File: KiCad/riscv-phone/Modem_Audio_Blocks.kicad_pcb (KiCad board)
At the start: 2 copper layers, 45.6 x 58.7 mm, 42 parts, among them J1 Conn_01x08, J10 SIM_Card, J2 Conn_01x02, J3 Conn_01x05, J4 Conn_02x03_Odd_Even, J5 Conn_01x02, J6 Conn_01x02, J7 Conn_01x02, J8 Conn_01x02, J9 SJ-3524-SMT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

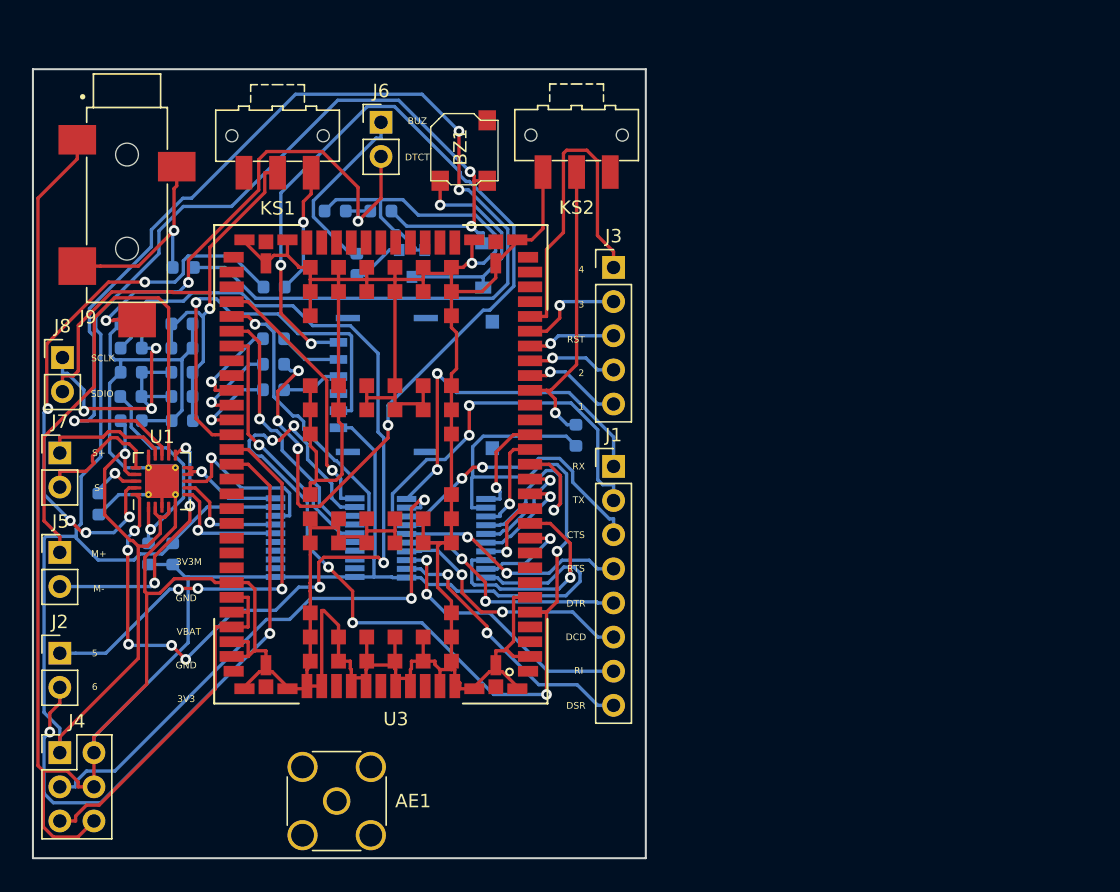
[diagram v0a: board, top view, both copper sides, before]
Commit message: Added GND planes and mounting holes
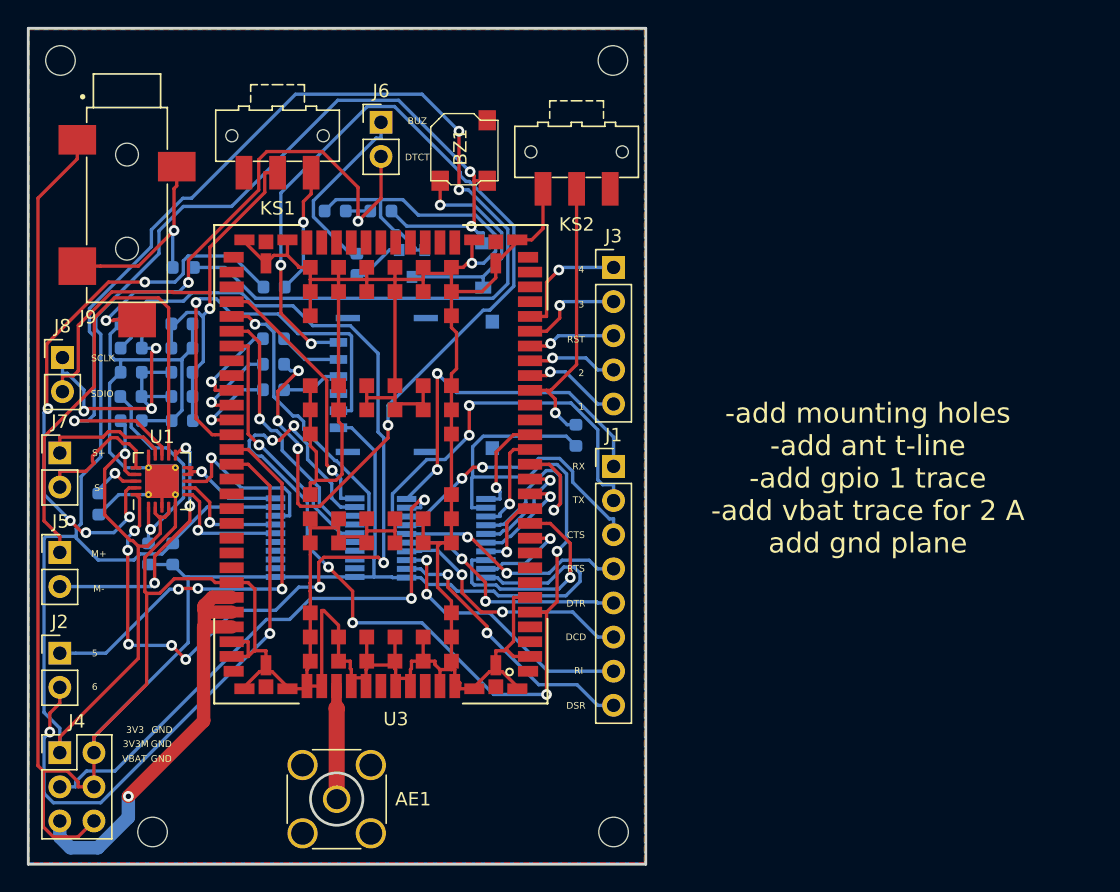
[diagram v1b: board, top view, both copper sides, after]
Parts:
- added ?: MountingHole_2.2mm_M2_ISO7380, MountingHole:MountingHole_2.2mm_M2_ISO7380, F.Cu at (106.0, 66.2)
- added ?: MountingHole_2.2mm_M2_ISO7380, MountingHole:MountingHole_2.2mm_M2_ISO7380, F.Cu at (147.2, 66.2)
- added ?: MountingHole_2.2mm_M2_ISO7380, MountingHole:MountingHole_2.2mm_M2_ISO7380, F.Cu at (147.2, 123.6)
- added ?: MountingHole_2.2mm_M2_ISO7380, MountingHole:MountingHole_2.2mm_M2_ISO7380, F.Cu at (112.9, 123.6)
- moved KS2 1.25 mm to (144.4, 73.0)
- moved AE1 0.14 mm to (126.6, 121.2)
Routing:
- net /ModemINDIV/GPIO4: track 25.3 -> 9.48 mm, vias 0 -> 1
- net Net-(AE1-Pad1): track 0.00 -> 8.44 mm
- net /ModemINDIV/VBAT: track 27.6 -> 33.1 mm, vias 0 -> 1
- net Net-(KS2-Pad2): track 22.4 -> 21.2 mm
- net GND: track 446.0 -> 444.8 mm
- added copper zone on B.Cu, net GND
- added copper zone on F.Cu, net GND
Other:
- board size 45.6 x 58.7 mm -> 45.9 x 62.2 mm
- board text added: "-add mounting holes -add ant t-line -add gpio 1 trace -add vbat trace for 2 A add gnd plane"

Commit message: Added GND vias
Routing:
- net GND: vias 1 -> 103
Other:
- outline, holes or cut-outs redrawn
- board text removed: "-add mounting holes -add ant t-line -add gpio 1 trace -add vbat trace for 2 A add gnd plane"

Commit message: Final PCB with added changes
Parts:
- removed ? (x4): MountingHole_2.2mm_M2_ISO7380, MountingHole:MountingHole_2.2mm_M2_ISO7380
- removed J5: Conn_01x02, Connector_PinHeader_2.54mm:PinHeader_1x02_P2.54mm_Vertical
- added Q2: MMBT3904, Package_TO_SOT_SMD:SOT-23, B.Cu at (133.4, 81.7)
- added R11: 1k, Resistor_SMD:R_0603_1608Metric, B.Cu at (133.4, 79.2)
- added R9: 1k, Resistor_SMD:R_0603_1608Metric, B.Cu at (133.2, 84.2)
- added m1: MountingHole_2.2mm_M2_ISO7380, MountingHole:MountingHole_2.2mm_M2_ISO7380, F.Cu at (146.8, 67.2)
- added m2: MountingHole_2.2mm_M2_ISO7380, MountingHole:MountingHole_2.2mm_M2_ISO7380, F.Cu at (105.9, 67.2)
- added m3: MountingHole_2.2mm_M2_ISO7380, MountingHole:MountingHole_2.2mm_M2_ISO7380, F.Cu at (105.9, 123.8)
- added m4: MountingHole_2.2mm_M2_ISO7380, MountingHole:MountingHole_2.2mm_M2_ISO7380, F.Cu at (146.8, 123.8)
- C1, C11, C14, C15, C4: moved to F.Cu
- J2: value Conn_01x02 -> Conn_01x03; footprint Connector_PinHeader_2.54mm:PinHeader_1x02_P2.54mm_Vertical -> Connector_PinHeader_2.54mm:PinHeader_1x03_P2.54mm_Vertical
- J3: value Conn_01x05 -> Conn_01x06; footprint Connector_PinHeader_2.54mm:PinHeader_1x05_P2.54mm_Vertical -> Connector_PinHeader_2.54mm:PinHeader_1x06_P2.54mm_Vertical
- moved C15 16.5 mm to (108.5, 96.7), turned to 270 degrees
- moved J2 15.3 mm to (105.9, 95.0)
- moved R6 13.7 mm to (123.8, 100.5)
- moved J10 11.7 mm to (129.1, 102.2)
- moved J6 11.6 mm to (118.6, 68.4)
- moved R8 11.5 mm to (123.8, 102.0)
- moved R4 10.5 mm to (119.5, 76.6), turned to 90 degrees
- moved D1 10.3 mm to (127.6, 78.6), turned to 0 degrees
- moved R7 10.3 mm to (123.8, 98.9)
- moved U2 9.75 mm to (134.6, 92.0)
- moved U4 9.70 mm to (125.2, 92.0)
- moved J7 9.60 mm to (105.9, 105.0)
- moved C16 8.72 mm to (117.8, 76.6), turned to 270 degrees
- moved R1 8.49 mm to (121.0, 76.6)
- moved C11 8.37 mm to (126.9, 76.3)
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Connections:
- J2 pad 1: /ModemINDIV/GPIO5 -> /AudioINDIV/SCLK
- J2 pad 2: /ModemINDIV/GPIO6 -> /AudioINDIV/SDIO
- J3 pad 1: /ModemINDIV/GPIO4 -> /ModemINDIV/STATUS
- J3 pad 2: /ModemINDIV/GPIO3 -> /ModemINDIV/GPIO4
- J3 pad 3: /ModemINDIV/RESET_N_1V8 -> /ModemINDIV/GPIO3
- J3 pad 4: /ModemINDIV/GPIO2 -> /ModemINDIV/RESET_N_1V8
- J3 pad 5: /ModemINDIV/GPIO1 -> /ModemINDIV/GPIO2
- J8 pad 1: /AudioINDIV/oMIC+ -> /AudioINDIV/oMIC-
- J8 pad 2: /AudioINDIV/oMIC- -> /AudioINDIV/oMIC+
- U1 pad 10: /AudioINDIV/BCLK -> /AudioINDIV/MCLK
- U3 pad 60: /ModemINDIV/GPIO5 -> /GPIO5
- U4 pad 1: Net-(U3-Pad50) -> /ModemINDIV/GPIO6
- U4 pad 15: Net-(U4-Pad15) -> /AudioINDIV/ADCOUT
- U4 pad 16: /AudioINDIV/ADCOUT -> /AudioINDIV/DACIN
- U4 pad 17: /AudioINDIV/DACIN -> /AudioINDIV/FS
- U4 pad 18: /AudioINDIV/FS -> /AudioINDIV/BCLK
- U4 pad 20: /AudioINDIV/BCLK -> /AudioINDIV/MCLK
- U4 pad 3: Net-(U3-Pad51) -> Net-(U3-Pad52)
- U4 pad 4: Net-(U3-Pad52) -> Net-(U3-Pad50)
- U4 pad 5: Net-(U3-Pad53) -> Net-(U3-Pad51)
- U4 pad 6: Net-(U4-Pad6) -> Net-(U3-Pad53)
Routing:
- net GND: track 444.8 -> 315.4 mm, vias 103 -> 143
- net Net-(C15-Pad2): track 91.6 -> 3.29 mm, vias 3 -> 0
- net Net-(J10-Pad7): track 79.3 -> 2.11 mm, vias 6 -> 0
- net /AudioINDIV/MIC+: track 75.0 -> 14.5 mm, vias 7 -> 1
- net +3V3: track 141.5 -> 99.4 mm, vias 3 -> 2
- net Net-(R7-Pad1): track 6.59 -> 38.8 mm, vias 1 -> 3
- net /ModemINDIV/GPIO5: track 31.2 -> 0.00 mm, vias 3 -> 0
- net /AudioINDIV/SDIO: track 36.9 -> 5.86 mm, vias 0 -> 1
- net /ModemINDIV/VDD_1V8: track 86.1 -> 62.7 mm, vias 6 -> 1
- net /ModemINDIV/GPIO6: track 45.2 -> 23.1 mm, vias 2 -> 1
- net /GPIO5: track 0.00 -> 20.4 mm, vias 0 -> 1
- net /AudioINDIV/MCLK: track 0.00 -> 20.4 mm, vias 0 -> 1
- net /ModemINDIV/STATUS: track 0.00 -> 16.7 mm
- net Net-(J10-Pad1): track 31.1 -> 15.0 mm
- net /AudioINDIV/HEADPHONE_DETECT: track 40.3 -> 24.3 mm, vias 3 -> 0
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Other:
- board size 45.9 x 62.2 mm -> 45.4 x 61 mm
- board text added: "STATUS"
- board text removed: "6"
